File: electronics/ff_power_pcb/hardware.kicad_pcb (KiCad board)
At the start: 4 copper layers, 60 x 37 mm, 60 parts, among them J1 Conn_01x01_Female, J2 Conn_01x01_Female, J3 Conn_01x07_Male, U3 TPS62095RGTR, U4 TPS62095RGTR, U5 TPS62095RGTR, U6 TPS62095RGTR, U7 AP131-25

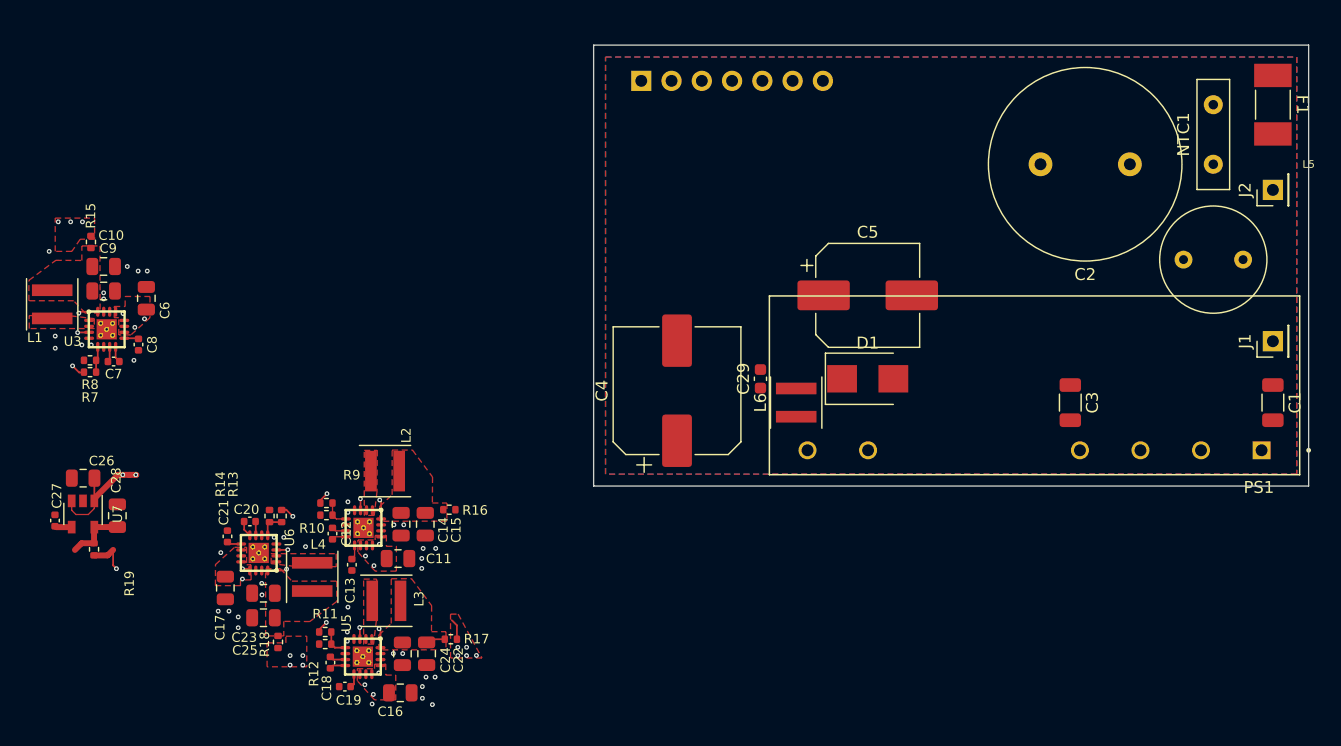
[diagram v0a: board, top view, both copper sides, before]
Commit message: Fit all the regulators into the power board.
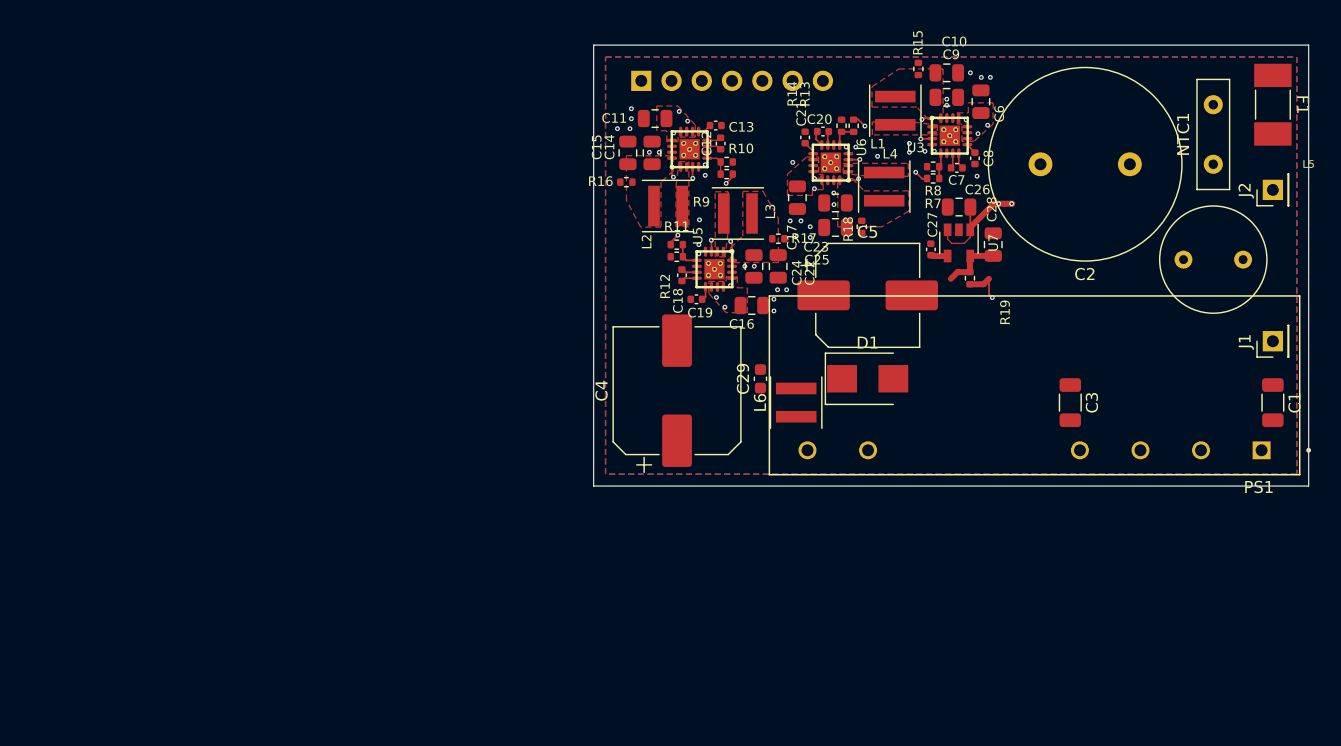
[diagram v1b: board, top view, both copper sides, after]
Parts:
- moved C26 76.9 mm to (116.7, 106.6)
- moved C27 76.9 mm to (114.3, 110.1)
- moved C28 76.9 mm to (119.5, 109.7)
- moved R19 76.9 mm to (117.6, 112.6)
- moved U7 76.9 mm to (116.7, 109.6)
- moved C10 72.6 mm to (115.6, 95.3)
- moved C7 72.6 mm to (116.5, 103.3)
- moved C9 72.6 mm to (115.6, 97.4)
- moved L1 72.6 mm to (111.3, 98.5)
- moved R7 72.6 mm to (114.5, 104.2)
- moved R8 72.6 mm to (114.5, 103.2)
- moved U3 72.6 mm to (115.9, 100.6)
- moved C6 71.9 mm to (118.5, 97.8)
- moved C8 71.9 mm to (118.0, 102.5)
- moved R15 70.9 mm to (113.2, 95.0)
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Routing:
- net +1V35: track 1.78 -> 0.00 mm, vias 5 -> 0
- net Net-(C22-Pad1): track 8.53 -> 7.27 mm
- net +3V3: vias 5 -> 2
- net GND: vias 40 -> 37
- net +1V1: vias 4 -> 0
- removed copper zone on F.Cu, net +1V1
- removed copper zone on F.Cu, net +1V35
- removed copper zone on F.Cu, net +3V3

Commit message: Leftover commit
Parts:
- moved C2 5.83 mm to (128.0, 98.0), turned to 270 degrees
- turned L5 to 180 degrees
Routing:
- net +3V3: track 10.8 -> 6.42 mm, vias 2 -> 0
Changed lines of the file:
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@@
     (thickness 1.6)
     (drawings 10)
-    (tracks 165)
+    (tracks 158)
     (zones 0)
     (modules 60)
@@
   )
   (module Bourns:RLB9012 (layer F.Cu)
-    (at 138 111)
+    (at 138 111 180)
     (fp_text reference L5 (at 8 -8) (layer F.SilkS)
       (effects (font (size 0.64 0.64) (thickness 0.015)))
@@
     (fp_circle (center 0 0) (end 4.5 0) (layer F.SilkS) (width 0.12))
     (fp_circle (center 0 0) (end 5 0) (layer F.CrtYd) (width 0.12))
-    (pad 2 thru_hole circle (at 2.5 0) (size 1.5 1.5) (drill 0.75) (layers *.Cu *.Mask)
+    (pad 2 thru_hole circle (at 2.5 0 180) (size 1.5 1.5) (drill 0.75) (layers *.Cu *.Mask)
       (net 39 "Net-(L5-Pad2)"))
-    (pad 1 thru_hole circle (at -2.5 0) (size 1.5 1.5) (drill 0.75) (layers *.Cu *.Mask)
+    (pad 1 thru_hole circle (at -2.5 0 180) (size 1.5 1.5) (drill 0.75) (layers *.Cu *.Mask)
       (net 33 "Net-(C1-Pad1)"))
     (model ${KIPRJMOD}/Bourns/rlb9012_short.stp
@@
   )
   (module Capacitor_THT:C_Radial_D16.0mm_H25.0mm_P7.50mm (layer F.Cu)
-    (at 131 103 180)
+    (at 128 98 270)
     (descr "C, Radial series, Radial, pin pitch=7.50mm, diameter=16mm, height=25mm, Non-Polar Electrolytic Capacitor")
     (tags "C Radial series Radial pin pitch 7.50mm diameter 16mm height 25mm Non-Polar Electrolytic Capacitor")
-    (fp_text reference C2 (at 3.75 -9.25) (layer F.SilkS)
-      (effects (font (size 1 1) (thickness 0.15)))
-    )
-    (fp_text value 33uF (at 3.75 9.25) (layer F.Fab)
+    (fp_text reference C2 (at 3.75 -9.25 90) (layer F.SilkS)
+      (effects (font (size 1 1) (thickness 0.15)))
+    )
+    (fp_text value 33uF (at 3.75 9.25 90) (layer F.Fab)
       (effects (font (size 1 1) (thickness 0.15)))
     )
@@
     (fp_circle (center 3.75 0) (end 11.87 0) (layer F.SilkS) (width 0.12))
     (fp_circle (center 3.75 0) (end 11.75 0) (layer F.Fab) (width 0.1))
-    (fp_text user %R (at 3.75 0) (layer F.Fab)
-      (effects (font (size 1 1) (thickness 0.15)))
-    )
-    (pad 2 thru_hole circle (at 7.5 0 180) (size 2 2) (drill 1) (layers *.Cu *.Mask)
+    (fp_text user %R (at 3.75 0 90) (layer F.Fab)
+      (effects (font (size 1 1) (thickness 0.15)))
+    )
+    (pad 2 thru_hole circle (at 7.5 0 270) (size 2 2) (drill 1) (layers *.Cu *.Mask)
       (net 34 "Net-(C2-Pad2)"))
-    (pad 1 thru_hole circle (at 0 0 180) (size 2 2) (drill 1) (layers *.Cu *.Mask)
+    (pad 1 thru_hole circle (at 0 0 270) (size 2 2) (drill 1) (layers *.Cu *.Mask)
       (net 35 "Net-(C2-Pad1)"))
     (model ${KISYS3DMOD}/Capacitor_THT.3dshapes/C_Radial_D16.0mm_H25.0mm_P7.50mm.wrl
@@
   (segment (start 115.70468 108.4976) (end 115.70468 108.187598) (width 0.15) (layer F.Cu) (net 4))
   (segment (start 117.60468 108.4976) (end 117.60468 108.292) (width 0.5) (layer F.Cu) (net 4))
-  (segment (start 117.60468 108.292) (end 119.58584 106.31084) (width 0.5) (layer F.Cu) (net 4))
-  (segment (start 119.58584 106.31084) (end 119.99224 106.31084) (width 0.5) (layer F.Cu) (net 4))
-  (segment (start 121.08444 106.31084) (end 121.13524 106.31084) (width 0.5) (layer F.Cu) (net 4))
-  (via (at 121.08444 106.31084) (size 0.4) (drill 0.2) (layers F.Cu B.Cu) (net 4))
-  (segment (start 120.55104 106.31084) (end 121.08444 106.31084) (width 0.5) (layer F.Cu) (net 4))
-  (segment (start 119.99224 106.31084) (end 120.55104 106.31084) (width 0.5) (layer F.Cu) (net 4))
-  (via (at 119.99224 106.31084) (size 0.4) (drill 0.2) (layers F.Cu B.Cu) (net 4))
   (segment (start 117.60468 108.4976) (end 117.60468 109.1302) (width 0.1) (layer F.Cu) (net 4))
   (segment (start 117.60468 109.1302) (end 117.09664 109.63824) (width 0.1) (layer F.Cu) (net 4))
@@
     (polygon
       (pts
-        (xy 145 129) (xy 87 129) (xy 87 94) (xy 145 94)
+        (xy 120 129) (xy 87 129) (xy 87 94) (xy 120 94)
       )
     )
@@
     (polygon
       (pts
-        (xy 145 129) (xy 87 129) (xy 87 94) (xy 145 94)
+        (xy 120 129) (xy 87 129) (xy 87 94) (xy 120 94)
       )
     )
@@
     (polygon
       (pts
-        (xy 145 129) (xy 87 129) (xy 87 94) (xy 145 94)
+        (xy 120 129) (xy 87 129) (xy 87 94) (xy 120 94)
       )
     )

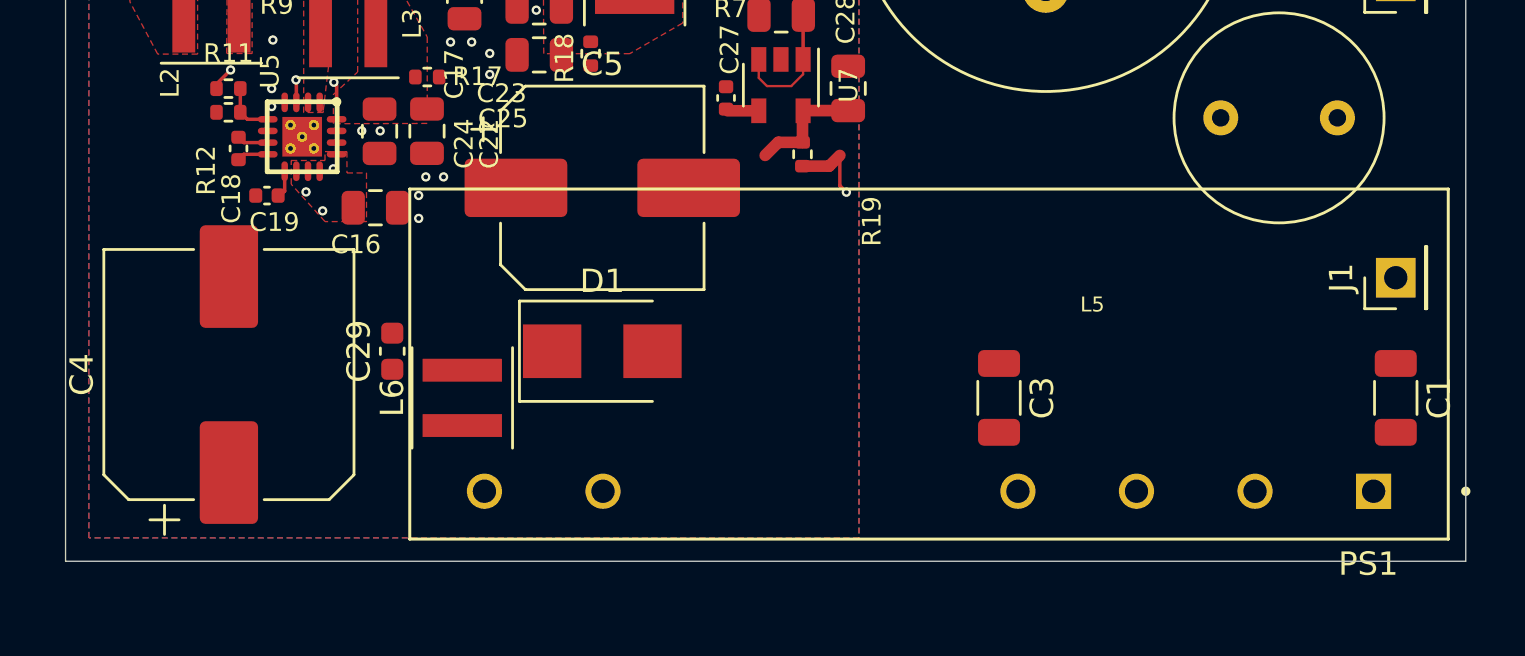
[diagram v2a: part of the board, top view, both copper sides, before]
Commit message: Changed out the 15W supply for a 5W.
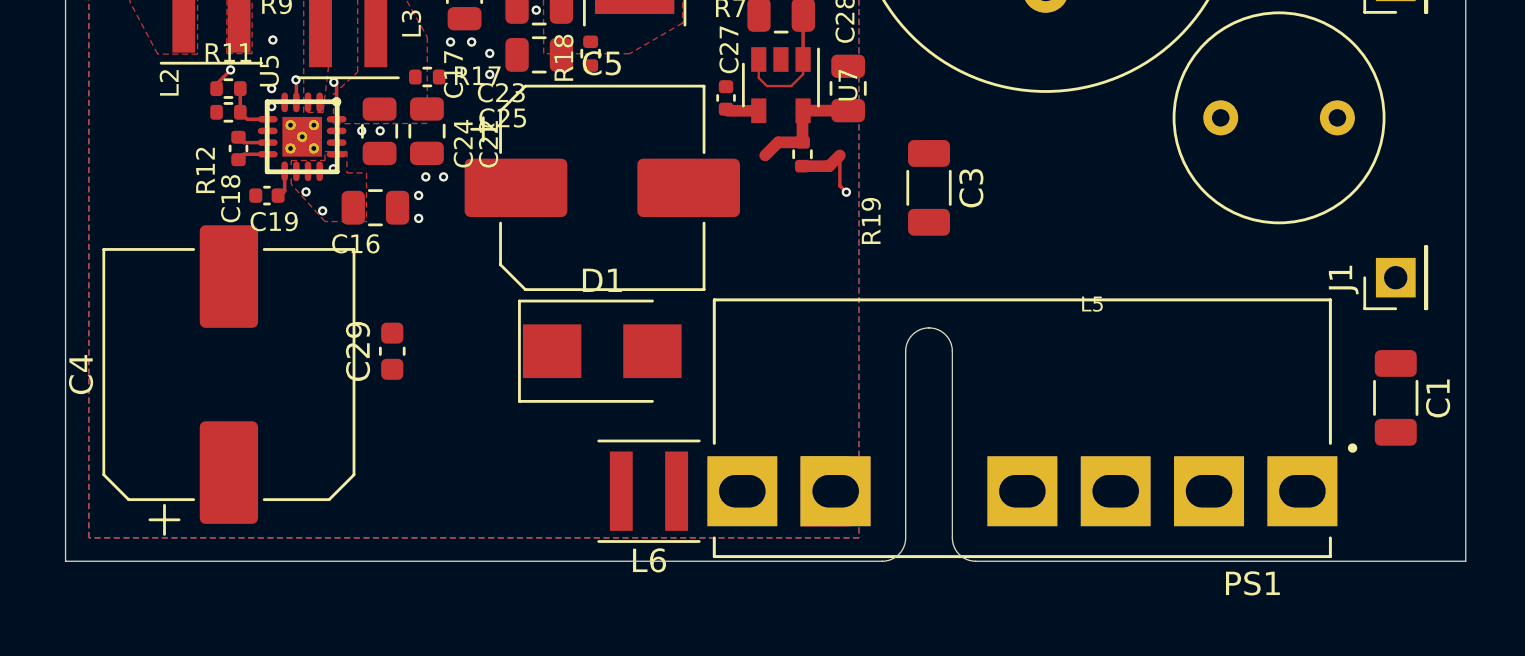
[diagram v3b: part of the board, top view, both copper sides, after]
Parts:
- PS1: value PBO-15C-5 -> PBO-5C-12; footprint CUI:CONV_PBO-15C-5 -> CUI:CONV_PBO-5C-12
- moved C3 9.49 mm to (123.0, 114.0)
- moved L6 8.94 mm to (111.0, 127.0), turned to 180 degrees
- moved PS1 4.00 mm to (127.0, 127.0)
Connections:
- J3 pad 1: (no net) -> Net-(J3-Pad1)
- J3 pad 2: (no net) -> Net-(J3-Pad2)
- J3 pad 3: (no net) -> Net-(J3-Pad3)
- J3 pad 4: (no net) -> Net-(J3-Pad4)
- J3 pad 5: (no net) -> Net-(J3-Pad5)
- J3 pad 6: (no net) -> Net-(J3-Pad6)
- J3 pad 7: (no net) -> Net-(J3-Pad7)
- PS1 pad 1: /AC_N -> Net-(L5-Pad2)
- PS1 pad 3: Net-(L5-Pad2) -> Net-(C2-Pad2)
- PS1 pad 5: Net-(C2-Pad1) -> GND
- R16 pad 1: (no net) -> +3V0
- R19 pad 1: (no net) -> +2V5
- U3 pad 4: (no net) -> Net-(U3-Pad4)
- U4 pad 4: (no net) -> Net-(U4-Pad4)
- U5 pad 4: (no net) -> Net-(U5-Pad4)
- U6 pad 4: (no net) -> Net-(U6-Pad4)
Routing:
- net +2V5: track 0.00 -> 3.48 mm, vias 0 -> 1
- net (no net): track 3.48 -> 0.00 mm, vias 1 -> 0
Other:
- outline, holes or cut-outs redrawn

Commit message: Working on the electronics for the FF revision.
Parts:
- C2: value 33uF -> 10uF; footprint Capacitor_THT:C_Radial_D16.0mm_H25.0mm_P7.50mm -> Capacitor_THT:C_Radial_D12.5mm_H20.0mm_P5.00mm
- C5: value 220uF -> 100uF; footprint Capacitor_SMD:CP_Elec_8x10.5 -> Capacitor_SMD:CP_Elec_6.3x5.8
- CY3: renamed from C3; value 2.2nF -> 1.0nF; footprint Capacitor_SMD:C_1206_3216Metric -> Capacitor_THT:C_Disc_D7.5mm_W5.0mm_P10.00mm
- L6: value 2.2uH -> 4.7uH; footprint Inductor_SMD:L_Coilcraft_XxL4020 -> Inductor_SMD:L_Coilcraft_XxL4030
- PS1: value PBO-5C-12 -> PBO-5C-5
- moved L6 8.06 mm to (103.0, 126.0), turned to 0 degrees
- moved C2 3.00 mm to (131.0, 98.0)
- moved CY3 1.41 mm to (122.0, 115.0), turned to 0 degrees
- moved NTC1 1.00 mm to (139.0, 103.0)
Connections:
- PS1 pad 3: Net-(C2-Pad2) -> Net-(C2-Pad1)
- PS1 pad 4: Net-(C2-Pad1) -> Net-(C2-Pad2)

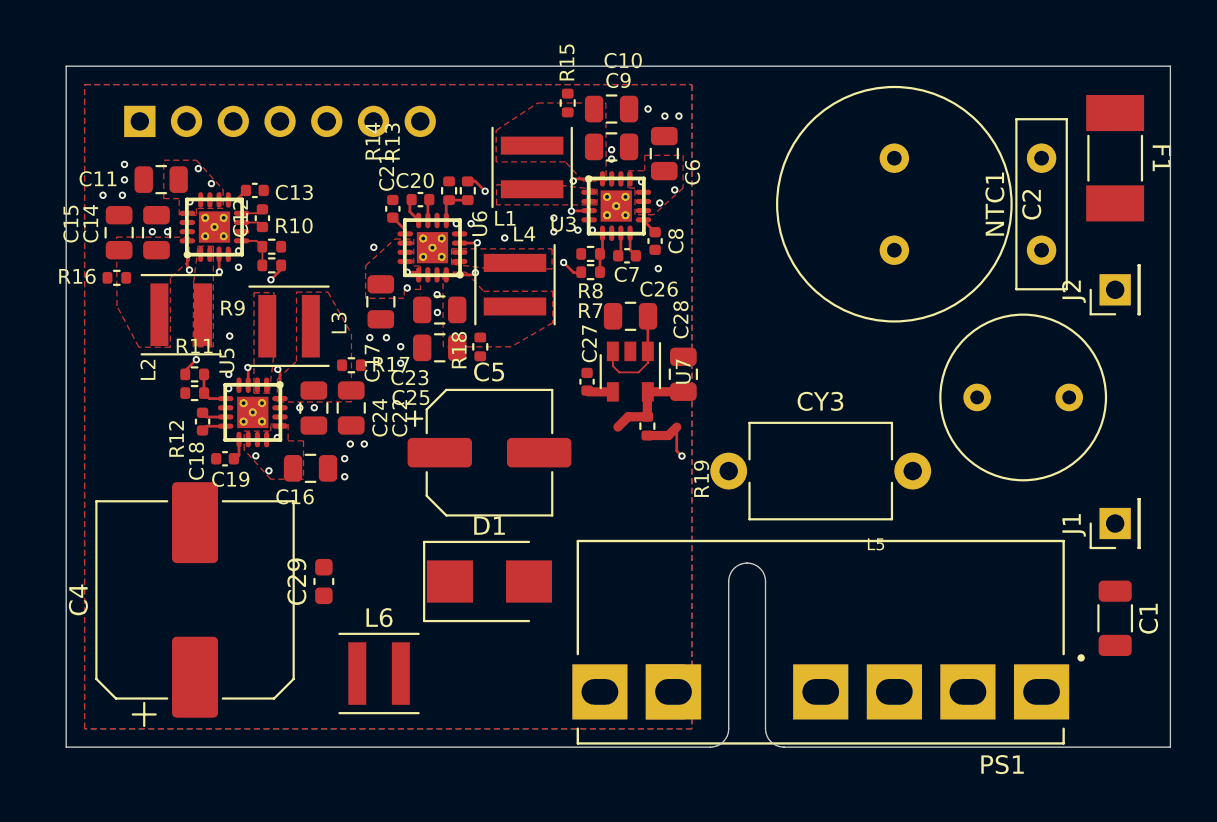
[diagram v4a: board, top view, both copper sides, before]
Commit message: Added step files, Working on the power board.
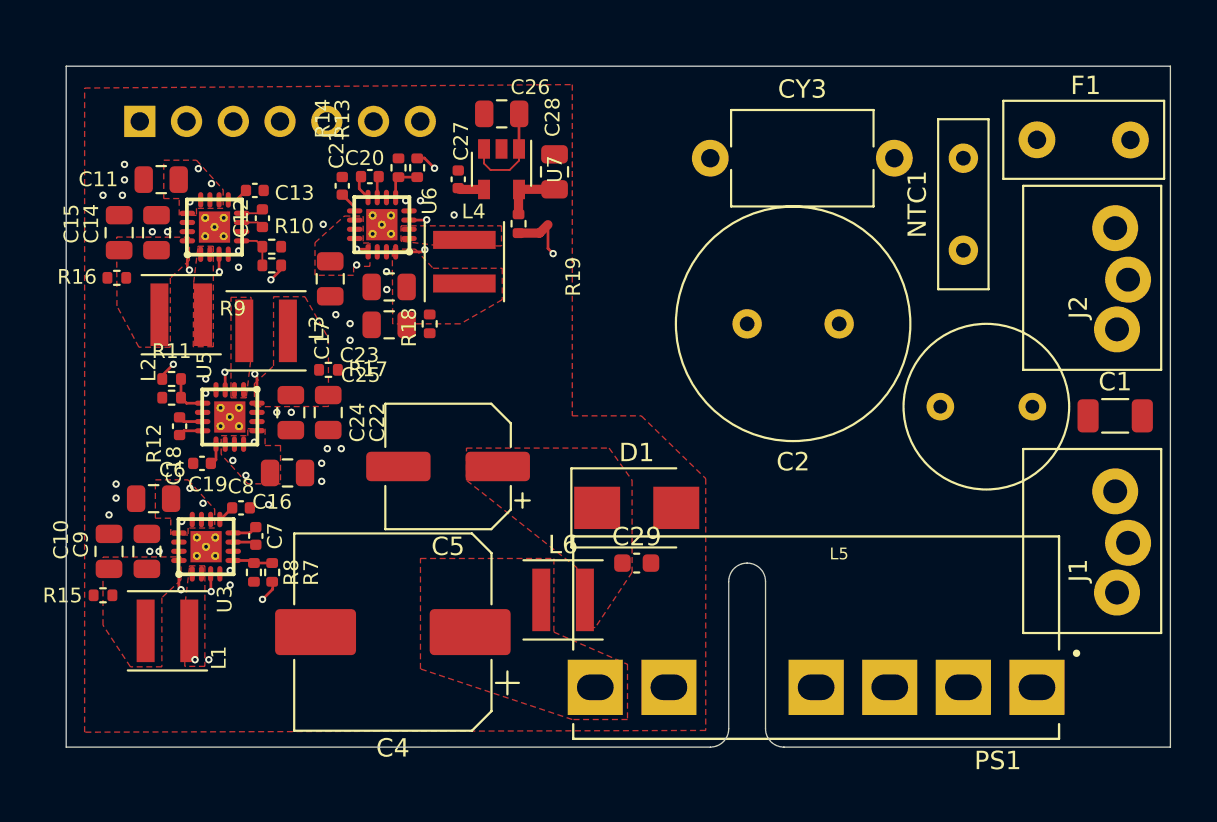
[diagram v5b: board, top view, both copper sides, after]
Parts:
- F1: footprint Fuse:Fuse_Littelfuse-NANO2-451_453 -> Fuse:Fuse_Littelfuse_395Series
- J1, J2: footprint Connector_PinHeader_2.54mm:PinHeader_1x01_P2.54mm_Vertical -> mains_blade:IRL_00
- moved R15 36.8 mm to (88.0, 121.8), turned to 0 degrees
- moved C10 36.4 mm to (88.3, 119.4), turned to 90 degrees
- moved C6 33.5 mm to (90.8, 116.5), turned to 180 degrees
- moved C9 33.5 mm to (90.4, 119.4), turned to 90 degrees
- moved L1 32.0 mm to (91.5, 123.7), turned to 180 degrees
- moved U3 29.0 mm to (93.6, 119.1), turned to 90 degrees
- moved C8 26.8 mm to (95.5, 117.0), turned to 0 degrees
- moved C7 25.3 mm to (96.3, 118.5), turned to 90 degrees
- moved R8 25.2 mm to (96.2, 120.5), turned to 270 degrees
- moved R7 23.8 mm to (97.2, 120.5), turned to 90 degrees
- moved C29 17.0 mm to (117.0, 120.0), turned to 0 degrees
- moved CY3 17.0 mm to (121.0, 98.0)
- moved C26 13.0 mm to (109.7, 95.6)
- moved C27 13.0 mm to (107.3, 99.1)
- moved C28 13.0 mm to (112.5, 98.7)
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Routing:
- net Net-(C28-Pad1): track 5.13 -> 3.30 mm
- net Net-(L1-Pad1): vias 0 -> 1
- net GND: vias 37 -> 34
- added copper zone on F.Cu, net Net-(C4-Pad1)
- removed copper zone on B.Cu, net GND
- removed copper zone on In2.Cu, net GND
